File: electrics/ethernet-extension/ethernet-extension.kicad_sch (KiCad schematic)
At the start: 44 parts, among them J1 Wuerth_7499010121A, J2 East, J3 West, U1 W5500, Y1 25MHz

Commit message: Added product numbers for cost calculation
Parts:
- C1, C2: Price 0.09 -> (none); Product https://www.mouser.de/ProductDetail/Kyocera-AVX/06035A180JA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 -> (none); manf# (none) -> 06035A180JAT4A; mouser# (none) -> 581-06035A180JAT4A
- C10, C18, C19, C3, C4, C7, C8, C9: Price 0.09 -> (none); Product https://www.mouser.de/ProductDetail/KEMET/C0603C104M4RACTU -> (none); manf# (none) -> C0603C104M4RACTU; mouser# (none) -> 80-C0603C104M4R
- C11: Price 0.10 -> (none); Product https://www.mouser.de/ProductDetail/Samsung-Electro-Mechani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 -> (none); manf# (none) -> CL10A106MQ8NNNC; mouser# (none) -> 187-CL10A106MQ8NNNC
- C12, C17, C5: Price 0.09 -> (none); Product https://www.mouser.de/ProductDetail/Kyocera-AVX/06031C103K4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 -> (none); manf# (none) -> 06031C103K4T2A; mouser# (none) -> 581-06031C103K4T2A
- C13, C14: Price 0.09 -> (none); Product https://www.mouser.de/ProductDetail/KEMET/C0603C682K5RACTU -> (none); manf# (none) -> C0603C682K5RACTU; mouser# (none) -> 80-C0603C682K5R
- C15: Price 0.09 -> (none); Product https://www.mouser.de/ProductDetail/Samsung-Electro-Mechani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 -> (none); manf# (none) -> CL10B223KB8NNNC; mouser# (none) -> 187-CL10B223KB8NNNC
- C16: Price 1.21 -> (none); Product https://www.mouser.de/ProductDetail/KEMET/C1812C103KGRACTU -> (none); manf# (none) -> C1812C103KGRACTU; mouser# (none) -> 80-C1812C103KGR
- C6: Price 0.09 -> (none); Product https://www.mouser.de/ProductDetail/Samsung-Electro-Mechani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 -> (none); manf# (none) -> CL10A475MQ8NNNC; mouser# (none) -> 187-CL10A475MQ8NNNC
- D1: Price 1.68 -> (none); Product https://www.mouser.de/ProductDetail/Bourns/CDNBS08-SLVU28-4 -> (none); manf# (none) -> CDNBS08-SLVU2.8-4; mouser# (none) -> 652-CDNBS08SLVU2.8-4
- D2: Price 0.12 -> (none); Product https://www.mouser.de/ProductDetail/Panjit/1N4148WS_R1_00001 -> (none); manf# (none) -> 1N4148WS_R1_00001; mouser# (none) -> 241-1N4148WSR100001
- FB1: Price 0.08 -> (none); Product https://www.mouser.de/ProductDetail/Laird-Performance-Mater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 -> (none); manf# (none) -> MG2029-121Y; mouser# (none) -> 652-MG2029-121Y
- G1: Price 0 -> (none); Product N/A -> (none)
- J1: Price 5.81 -> (none); Product https://www.mouser.de/ProductDetail/Wurth-Elektronik/749901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 -> (none); manf# (none) -> 7499010121A; mouser# (none) -> 710-7499010121A
- J2, J3: Price 2.40 -> (none); Product https://www.mouser.de/ProductDetail/Preci-dip/801-87-014-53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 -> (none); manf# (none) -> 801-87-014-53-001101; mouser# (none) -> 437-8018701453001101
- R1, R2: Price 0.09 -> (none); Product https://www.mouser.de/ProductDetail/Bourns/CR0603-FX-3300EL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 -> (none); manf# (none) -> CR0603-FX-3300ELF; mouser# (none) -> 652-CR0603FX-3300ELF
- R14, R15: Price 0.09 -> (none); Product https://www.mouser.de/ProductDetail/Panasonic/ERJ-3EKF82R0V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 -> (none); manf# (none) -> ERJ-3EKF82R0V; mouser# (none) -> 667-ERJ-3EKF82R0V
- R16: Price 0.09 -> (none); Product https://www.mouser.de/ProductDetail/YAGEO/RC0603FR-1310RL?q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 -> (none); manf# (none) -> RC0603FR-1310RL; mouser# (none) -> 603-RC0603FR-1310RL
- R17, R18: Price 0.09 -> (none); Product https://www.mouser.de/ProductDetail/Panasonic/ERJ-3EKF49R9V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 -> (none); manf# (none) -> ERJ-3EKF49R9V; mouser# (none) -> 667-ERJ-3EKF49R9V
- R19, R3, R4, R5, R6, R7: Product https://www.mouser.de/ProductDetail/Bourns/CR0603AFX-1002EA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 -> (none); manf# (none) -> CR0603AFX-1002EAS; mouser# (none) -> 652-CR0603AFX1002EAS
- R8: Product https://www.mouser.de/ProductDetail/Bourns/CMP0603-FX-1004E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 -> (none); manf# (none) -> CMP0603-FX-1004ELF; mouser# (none) -> 652-CMP0603-FX-1004L
- R9: Price 0.09 -> (none); Product https://www.mouser.de/ProductDetail/Bourns/CR0603-FX-1242EL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 -> (none); manf# (none) -> CR0603-FX-1242ELF; mouser# (none) -> 652-CR0603FX-1242ELF
- U1: Price 3.44 -> (none); Product https://www.mouser.de/ProductDetail/WIZnet/W5500 -> (none); manf# (none) -> W5500; mouser# (none) -> 950-W5500
- Y1: Price 0.98 -> (none); Product https://www.mouser.de/ProductDetail/ECS/ECS-250-18-23A-TR -> (none); manf# (none) -> ECS-250-18-23A-TR; mouser# (none) -> 520-250-18-23A

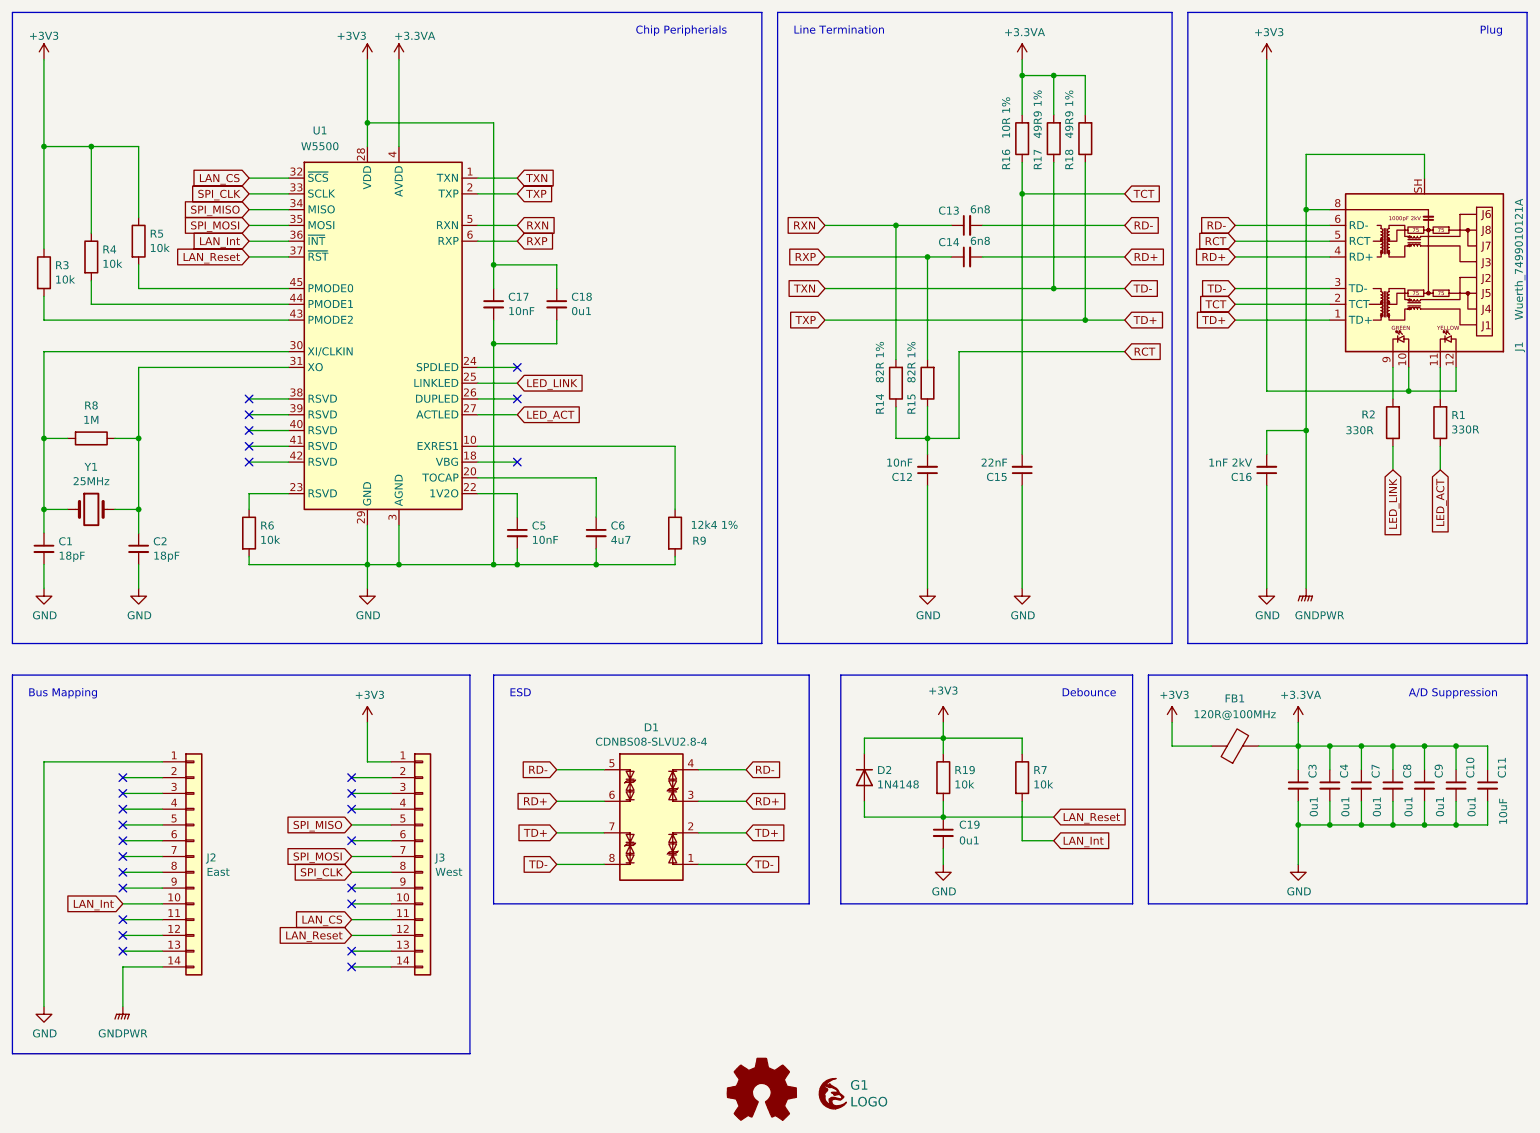
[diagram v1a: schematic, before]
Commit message: Fix all ERC and DRC warnings during build
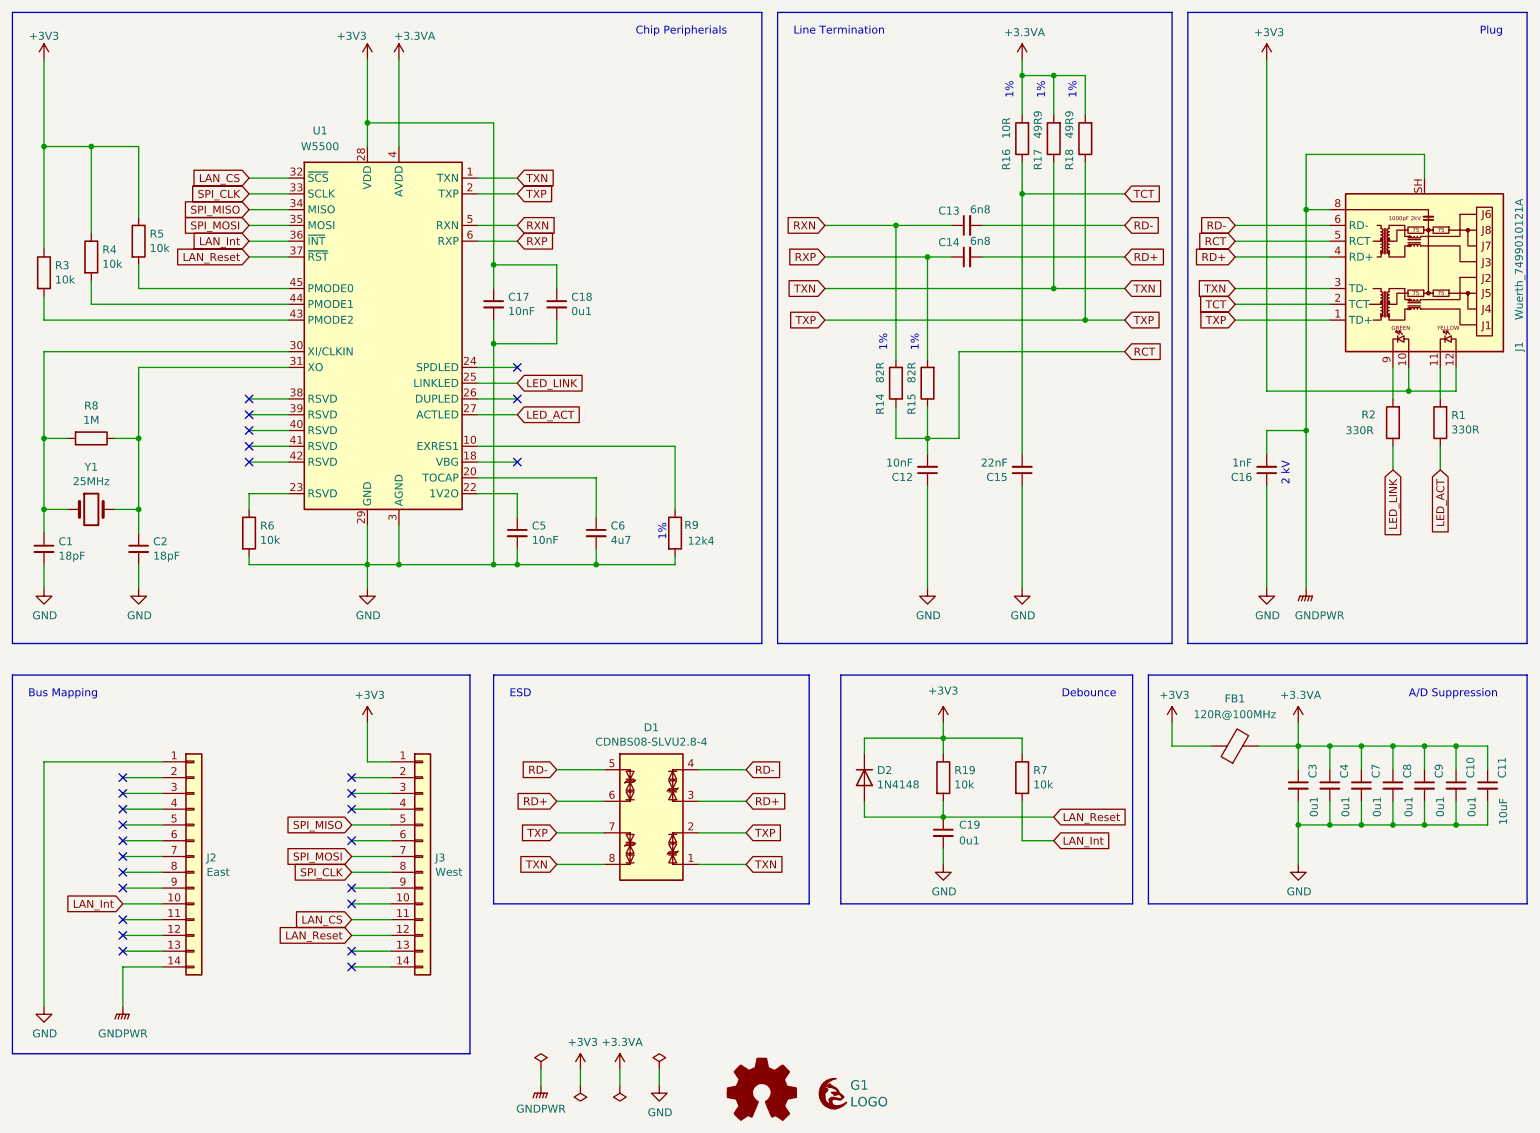
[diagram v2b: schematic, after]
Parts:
- C16: value 1nF 2kV -> 1nF
- R14, R15: value 82R 1% -> 82R
- R16: value 10R 1% -> 10R
- R17, R18: value 49R9 1% -> 49R9
- R9: value 12k4 1% -> 12k4
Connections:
- net TD+ renamed TXP
- net TD- renamed TXN
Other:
- note added: "1%"
- note added: "2 kV"
